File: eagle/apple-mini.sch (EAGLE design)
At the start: 20 parts, among them J1 USBMICROB, J2 JTAG, J3 CON2X22, U1 FT240XS, U2 TPS2082D

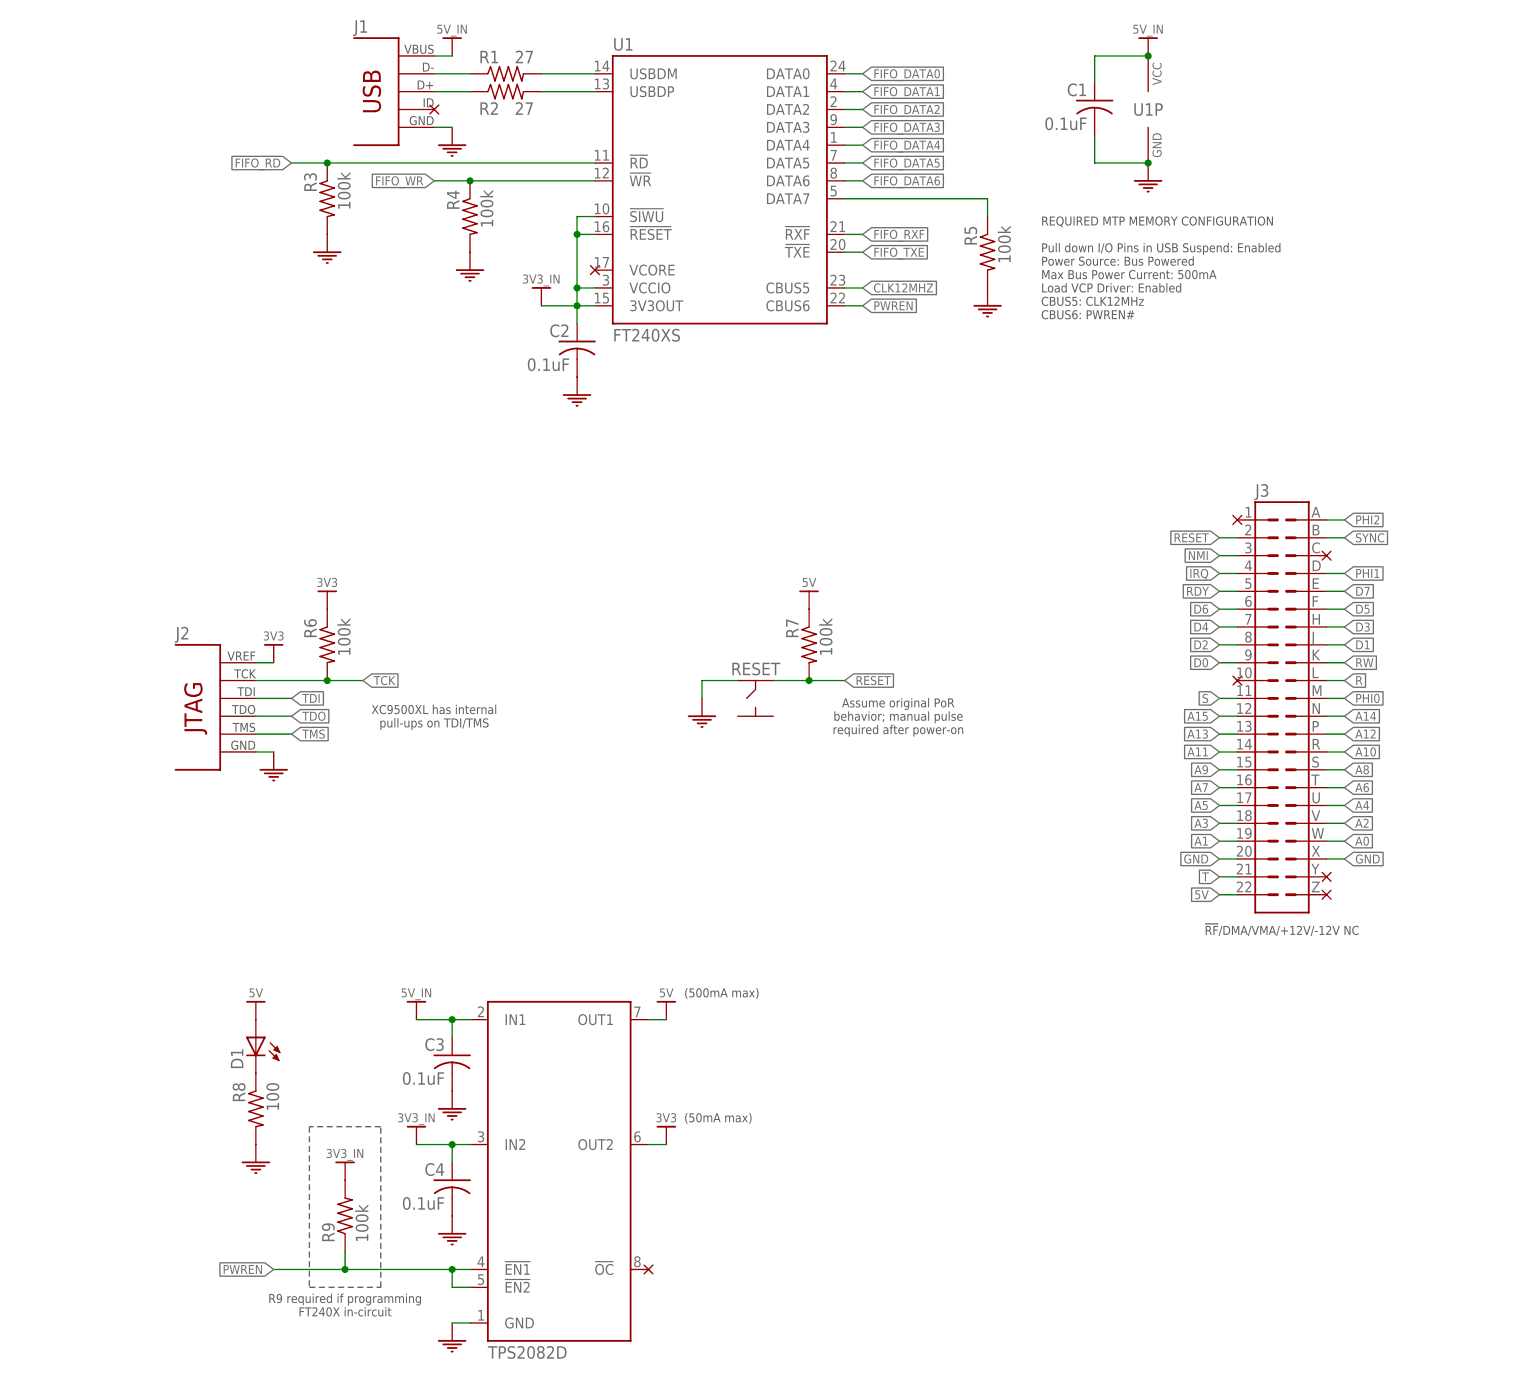
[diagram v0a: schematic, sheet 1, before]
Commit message: Rename project; sundry style updates
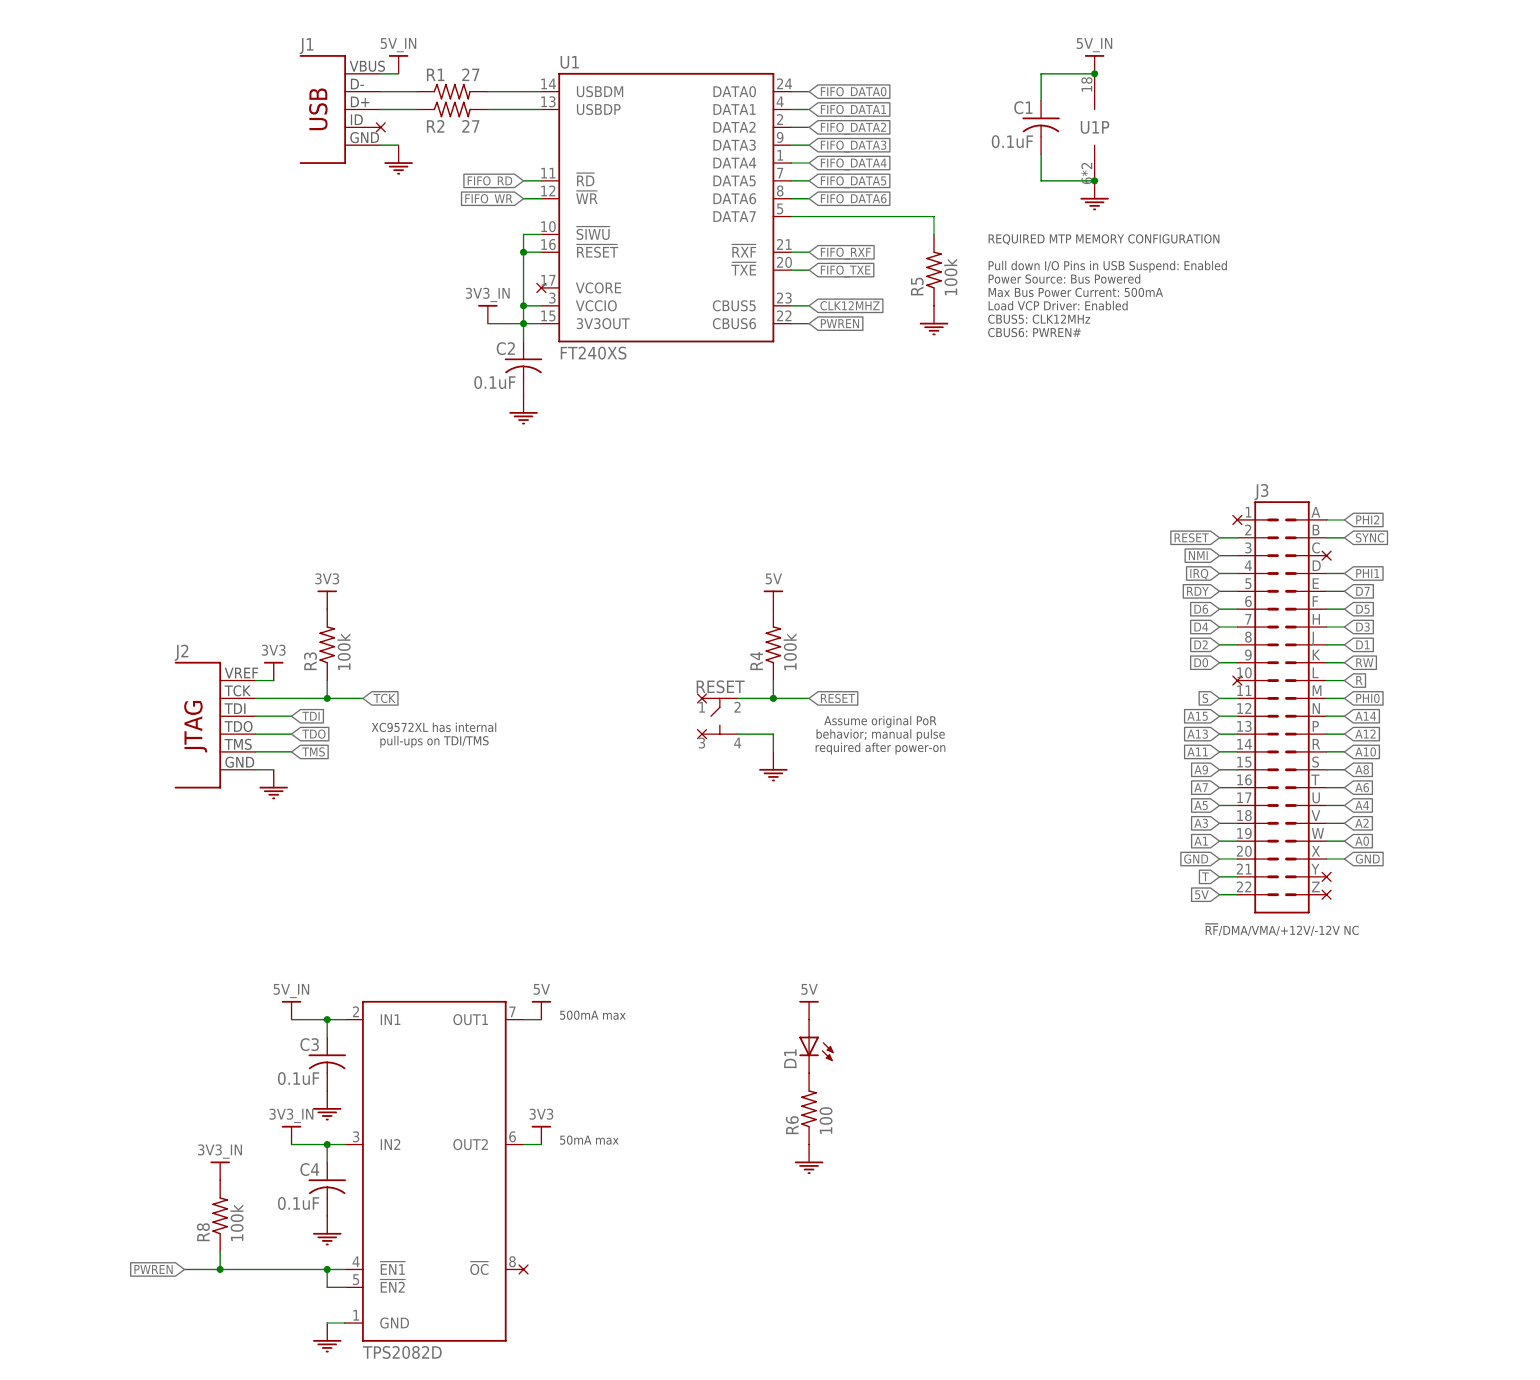
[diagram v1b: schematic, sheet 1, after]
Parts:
- removed R7, R9: 100k, rcl:R-US_R0805
- J1: value USBMICROB -> USBMICRO; device apple-idun:USBMICROB -> apple-mini:USBMICRO
- J2: device apple-idun:JTAG -> apple-mini:JTAG
- J3: value CON2X22 -> RBM22DRTN; device apple-idun:CON2X22 -> apple-mini:RBM22DRTN
- R6: value 100k -> 100
- R8: value 100 -> 100k
- RESET: device apple-idun:TACTSW -> apple-mini:TACTSW
- U1: device apple-idun:FT240XS -> apple-mini:FT240XS
- U2: device apple-idun:TPS2082D -> apple-mini:TPS2082D
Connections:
- net 3V3: now also R3.2, R4.2; no longer R6.1
- net 3V3_IN: now also R8.2; no longer R9.2
- net 5V: no longer R7.1
- net FIFO_RD: no longer R3.1
- net FIFO_WR: no longer R4.1
- net GND: now also R5.1, R6.1, RESET.4; no longer R3.2, R4.2, R5.2, R8.2, RESET.1
- net N$1: now also R6.2; no longer R8.1
- net N$2: now also R5.2; no longer R5.1
- net PWREN: now also R8.1; no longer R9.1
- net RESET: now also R4.1; no longer R7.2
- net TCK: now also R3.1; no longer R6.2
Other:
- note added: "500mA max"
- note added: "50mA max"
- note added: "XC9572XL has internal pull-ups on TDI/TMS"
- note removed: "(500mA max)"
- note removed: "(50mA max)"
- note removed: "R9 required if programming FT240X in-circuit"
- note removed: "XC9500XL has internal pull-ups on TDI/TMS"
- moved on the sheet: C1, C2, C3, C4, D1, J1, J2, R1, R2, R3, R4, R5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

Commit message: Add CPLD and clear switch
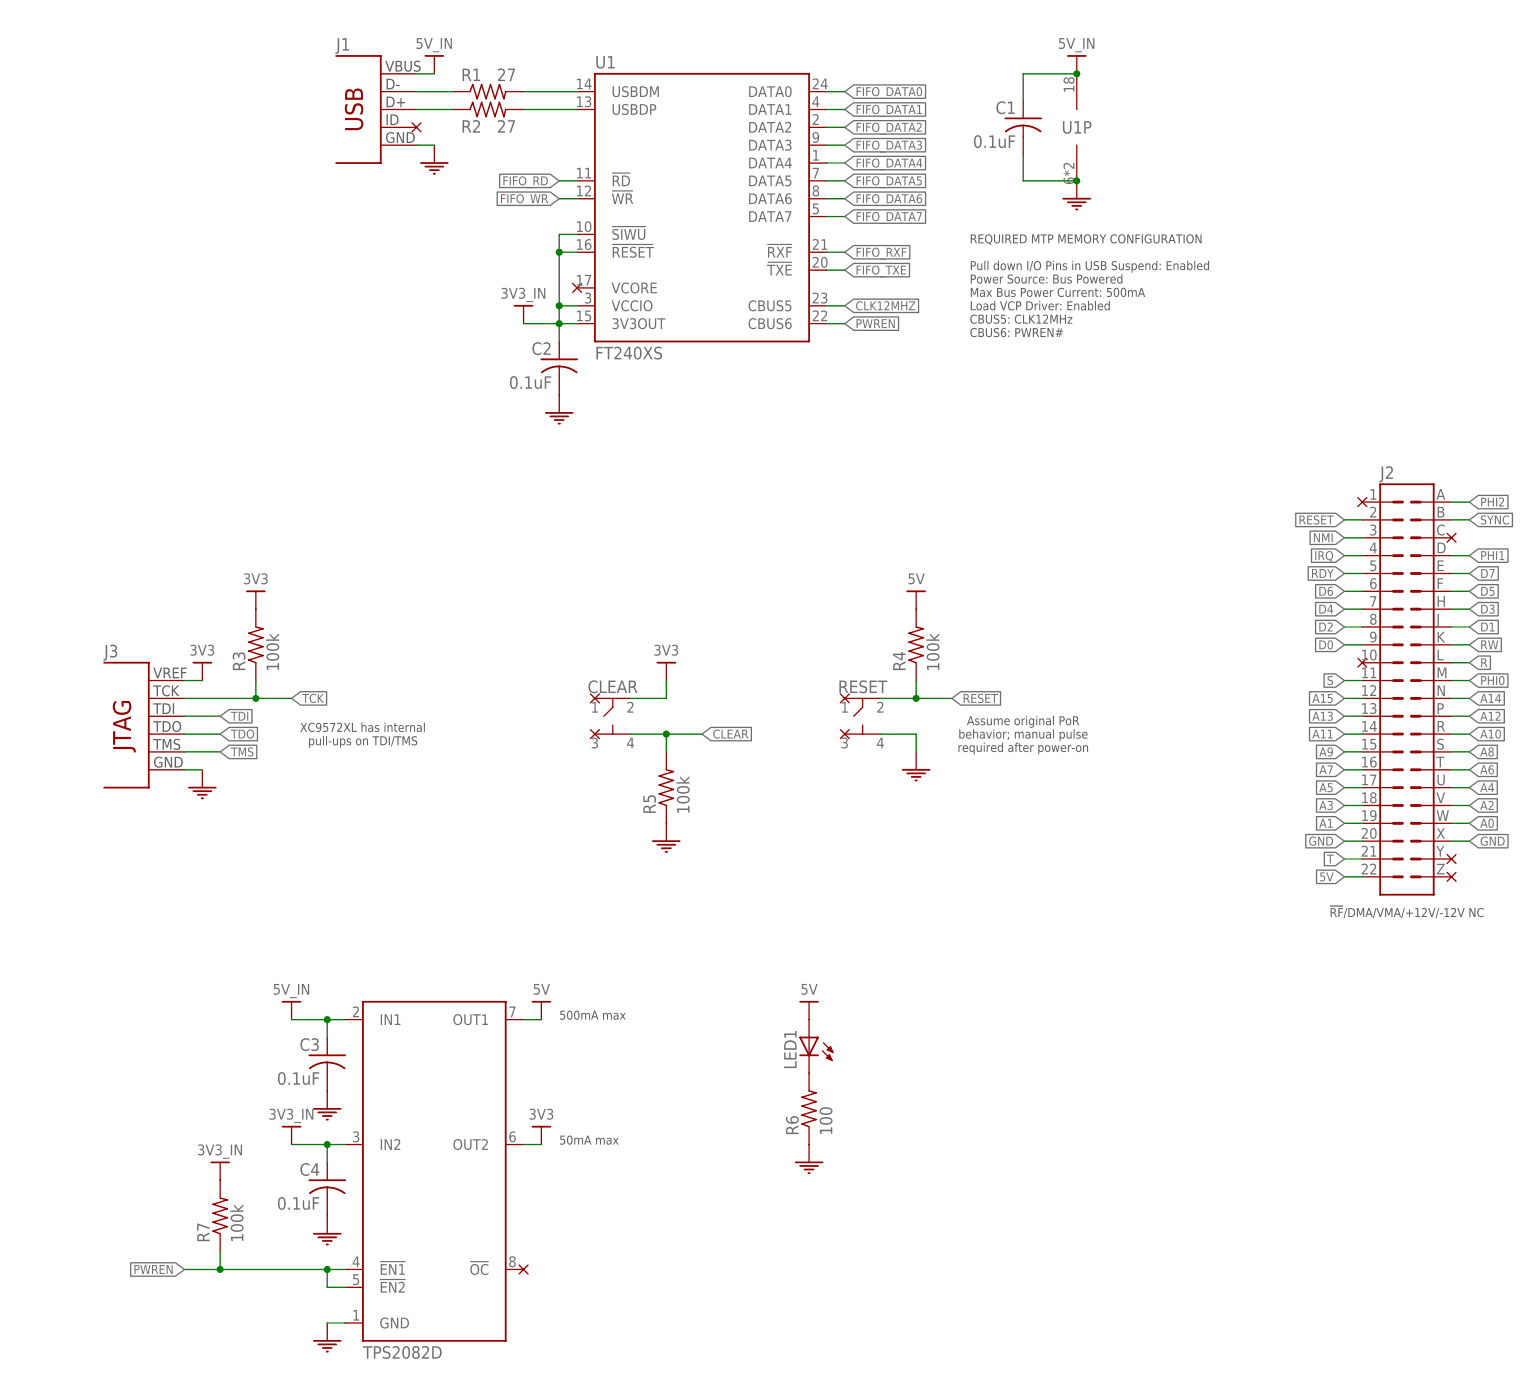
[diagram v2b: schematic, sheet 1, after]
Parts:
- added C5, C6, C7, C8: 0.1uF, rcl:C-USC0805
- added CLEAR: TACTSW, apple-mini:TACTSW
- added U3: XC9572XL-10VQ64, apple-mini:XC9572XL-10VQ64
- J2: value JTAG -> RBM22DRTN; device apple-mini:JTAG -> apple-mini:RBM22DRTN
- J3: value RBM22DRTN -> JTAG; device apple-mini:RBM22DRTN -> apple-mini:JTAG
- renumbered D1 to LED1, R8 to R7
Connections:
- removed net N$2: R5.2, U1G$1.DATA7
- new net CA1: U3G$1.P52
- new net CA2: U3G$1.P56
- new net CB1: U3G$1.P19
- new net CB2: U3G$1.P40
- new net CLEAR: CLEAR.4, R5.2, U3G$1.P31
- new net DA: U3G$1.P20
- new net FIFO_DATA7: U1G$1.DATA7, U3G$1.P39
- new net PA0: U3G$1.P6
- new net PA1: U3G$1.P60
- new net PA2: U3G$1.P58
- new net PA3: U3G$1.P62
- new net PA4: U3G$1.P63
- new net PA5: U3G$1.GSR/P64
- new net PA6: U3G$1.P4
- new net PB0: U3G$1.P61
- new net PB1: U3G$1.P5/GTS1
- new net PB2: U3G$1.P46
- new net PB3: U3G$1.P7
- new net PB4: U3G$1.P11
- new net PB5: U3G$1.P13
- new net PB6: U3G$1.P12
- new net X: U3G$1.P34
- new net Y: U3G$1.P42
- new net Z: U3G$1.P38
- net 3V3: now also C5.1, C6.1, C7.1, C8.1, CLEAR.2, J3.VREF, U3PA.VCC, U3PB.VCC, U3PC.VCC, U3PD.VCC; no longer J2.VREF
- net 5V: now also J2.22; no longer J3.22
- net A0: now also J2.W, U3G$1.P57; no longer J3.W
- net A1: now also J2.19, U3G$1.P59; no longer J3.19
- net A10: now also J2.R; no longer J3.R
- net A11: now also J2.14; no longer J3.14
- net A12: now also J2.P; no longer J3.P
- net A13: now also J2.13; no longer J3.13
- net A14: now also J2.N; no longer J3.N
- net A15: now also J2.12; no longer J3.12
- net A2: now also J2.V, U3G$1.P50; no longer J3.V
- net A3: now also J2.18, U3G$1.P2/GTS2; no longer J3.18
- net A4: now also J2.U; no longer J3.U
- net A5: now also J2.17; no longer J3.17
- net A6: now also J2.T; no longer J3.T
- net A7: now also J2.16; no longer J3.16
- net A8: now also J2.S; no longer J3.S
- net A9: now also J2.15; no longer J3.15
- net CLK12MHZ: now also U3G$1.P16/GCK2
- net D0: now also J2.9; no longer J3.9
- net D1: now also J2.J; no longer J3.J
- net D2: now also J2.8; no longer J3.8
- net D3: now also J2.H; no longer J3.H
- net D4: now also J2.7; no longer J3.7
- net D5: now also J2.F; no longer J3.F
- net D6: now also J2.6; no longer J3.6
- net D7: now also J2.E; no longer J3.E
- net FIFO_DATA0: now also U3G$1.P43
- net FIFO_DATA1: now also U3G$1.P44
- net FIFO_DATA2: now also U3G$1.P49
- net FIFO_DATA3: now also U3G$1.P51
- net FIFO_DATA4: now also U3G$1.P8
- net FIFO_DATA5: now also U3G$1.P9
- net FIFO_DATA6: now also U3G$1.P10
- net FIFO_RD: now also U3G$1.P22
- net FIFO_RXF: now also U3G$1.P48
- net FIFO_TXE: now also U3G$1.P45
- net FIFO_WR: now also U3G$1.P18
- net GND: now also C5.2, C6.2, C7.2, C8.2, J2.20, J2.X, J3.GND, U3G$1.P15/GCK1, U3G$1.P17/GCK3, U3G$1.P23, U3G$1.P25, U3G$1.P32, U3G$1.P36, U3PA.GND, U3PB.GND, U3PC.GND, U3PD.GND; no longer J2.GND, J3.20, J3.X
- net IRQ: now also J2.4; no longer J3.4
- net NMI: now also J2.3; no longer J3.3
- net PHI0: now also J2.M, U3G$1.P24; no longer J3.M
- net PHI1: now also J2.D; no longer J3.D
- net PHI2: now also J2.A, U3G$1.P47; no longer J3.A
- net R: now also J2.L, U3G$1.P27; no longer J3.L
- net RDY: now also J2.5; no longer J3.5
- net RESET: now also J2.2, U3G$1.P1; no longer J3.2
- net RW: now also J2.K; no longer J3.K
- net S: now also J2.11, U3G$1.P33; no longer J3.11
- net SYNC: now also J2.B; no longer J3.B
- net T: now also J2.21, U3G$1.P35; no longer J3.21
- net TCK: now also J3.TCK, U3G$1.TCK; no longer J2.TCK
- net TDI: now also J3.TDI, U3G$1.TDI; no longer J2.TDI
- net TDO: now also J3.TDO, U3G$1.TDO; no longer J2.TDO
- net TMS: now also J3.TMS, U3G$1.TMS; no longer J2.TMS
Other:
- moved on the sheet: C1, C2, J1, R1, R2, R3, R4, R5, RESET, U1, U1P

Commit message: Add schmitt buffer on clear/reset
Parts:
- added C10, C11, C9: 0.1uF, rcl:C-USC0805
- added R8: 100, rcl:R-US_R0805
- added R9: 100k, rcl:R-US_R0805
- added U4: XC9572XL-10VQ64, apple-mini:XC9572XL-10VQ64
- C4, C5: value 0.1uF -> 0.22uF
- R7: value 100k -> 100
- U2: value TPS2082D -> SN74LVC2G17DBV; device apple-mini:TPS2082D -> apple-mini:SN74LVC2G17DBV
- U3: value XC9572XL-10VQ64 -> TPS2082D; device apple-mini:XC9572XL-10VQ64 -> apple-mini:TPS2082D
- renumbered LED1 to D1
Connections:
- new net N$2: CLEAR.2, R6.1
- new net N$3: R7.1, RESET.2
- new net N$4: C4.1, R4.1, R6.2, U2A.A
- new net N$5: C5.1, R5.1, R7.2, U2B.A
- net 3V3: now also C10.1, C11.1, C2.1, C9.1, R5.2, U2P.VCC, U3.OUT2, U4PA.VCC, U4PB.VCC, U4PC.VCC, U4PD.VCC; no longer C5.1, C6.1, C7.1, CLEAR.2, U2.OUT2, U3PA.VCC, U3PB.VCC, U3PC.VCC, U3PD.VCC
- net 3V3_IN: now also C3.1, C7.1, R9.2, U3.IN2; no longer C2.1, C4.1, R7.2, U2.IN2
- net 5V: now also U3.OUT1; no longer U2.OUT1
- net 5V_IN: now also C6.1, U3.IN1; no longer C3.1, U2.IN1
- net A0: now also U4G$1.P57; no longer U3G$1.P57
- net A1: now also U4G$1.P59; no longer U3G$1.P59
- net A2: now also U4G$1.P50; no longer U3G$1.P50
- net A3: now also U4G$1.P2/GTS2; no longer U3G$1.P2/GTS2
- net CA1: now also U4G$1.P52; no longer U3G$1.P52
- net CA2: now also U4G$1.P56; no longer U3G$1.P56
- net CB1: now also U4G$1.P19; no longer U3G$1.P19
- net CB2: now also U4G$1.P40; no longer U3G$1.P40
- net CLEAR: now also U2A.Y, U4G$1.P31; no longer CLEAR.4, R5.2, U3G$1.P31
- net CLK12MHZ: now also U4G$1.P16/GCK2; no longer U3G$1.P16/GCK2
- net DA: now also U4G$1.P20; no longer U3G$1.P20
- net FIFO_DATA0: now also U4G$1.P43; no longer U3G$1.P43
- net FIFO_DATA1: now also U4G$1.P44; no longer U3G$1.P44
- net FIFO_DATA2: now also U4G$1.P49; no longer U3G$1.P49
- net FIFO_DATA3: now also U4G$1.P51; no longer U3G$1.P51
- net FIFO_DATA4: now also U4G$1.P8; no longer U3G$1.P8
- net FIFO_DATA5: now also U4G$1.P9; no longer U3G$1.P9
- net FIFO_DATA6: now also U4G$1.P10; no longer U3G$1.P10
- net FIFO_DATA7: now also U4G$1.P39; no longer U3G$1.P39
- net FIFO_RD: now also U4G$1.P22; no longer U3G$1.P22
- net FIFO_RXF: now also U4G$1.P48; no longer U3G$1.P48
- net FIFO_TXE: now also U4G$1.P45; no longer U3G$1.P45
- net FIFO_WR: now also U4G$1.P18; no longer U3G$1.P18
- net GND: now also C10.2, C11.2, C9.2, CLEAR.4, R8.1, U2P.GND, U3.GND, U4G$1.P15/GCK1, U4G$1.P17/GCK3, U4G$1.P23, U4G$1.P25, U4G$1.P32, U4G$1.P36, U4PA.GND, U4PB.GND, U4PC.GND, U4PD.GND; no longer R5.1, R6.1, U2.GND, U3G$1.P15/GCK1, U3G$1.P17/GCK3, U3G$1.P23, U3G$1.P25, U3G$1.P32, U3G$1.P36, U3PA.GND, U3PB.GND, U3PC.GND, U3PD.GND
- net N$1: now also R8.2; no longer R6.2
- net PA0: now also U4G$1.P6; no longer U3G$1.P6
- net PA1: now also U4G$1.P60; no longer U3G$1.P60
- net PA2: now also U4G$1.P58; no longer U3G$1.P58
- net PA3: now also U4G$1.P62; no longer U3G$1.P62
- net PA4: now also U4G$1.P63; no longer U3G$1.P63
- net PA5: now also U4G$1.GSR/P64; no longer U3G$1.GSR/P64
- net PA6: now also U4G$1.P4; no longer U3G$1.P4
- net PB0: now also U4G$1.P61; no longer U3G$1.P61
- net PB1: now also U4G$1.P5/GTS1; no longer U3G$1.P5/GTS1
- net PB2: now also U4G$1.P46; no longer U3G$1.P46
- net PB3: now also U4G$1.P7; no longer U3G$1.P7
- net PB4: now also U4G$1.P11; no longer U3G$1.P11
- net PB5: now also U4G$1.P13; no longer U3G$1.P13
- net PB6: now also U4G$1.P12; no longer U3G$1.P12
- net PHI0: now also U4G$1.P24; no longer U3G$1.P24
- net PHI2: now also U4G$1.P47; no longer U3G$1.P47
- net PWREN: now also R9.1, U3.!EN1, U3.!EN2; no longer R7.1, U2.!EN1, U2.!EN2
- net R: now also U4G$1.P27; no longer U3G$1.P27
- net RESET: now also U2B.Y, U4G$1.P1; no longer R4.1, RESET.2, U3G$1.P1
- net S: now also U4G$1.P33; no longer U3G$1.P33
- net T: now also U4G$1.P35; no longer U3G$1.P35
- net TCK: now also U4G$1.TCK; no longer U3G$1.TCK
- net TDI: now also U4G$1.TDI; no longer U3G$1.TDI
- net TDO: now also U4G$1.TDO; no longer U3G$1.TDO
- net TMS: now also U4G$1.TMS; no longer U3G$1.TMS
- net X: now also U4G$1.P34; no longer U3G$1.P34
- net Y: now also U4G$1.P42; no longer U3G$1.P42
- net Z: now also U4G$1.P38; no longer U3G$1.P38
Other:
- note removed: "Assume original PoR behavior; manual pulse required after power-on"
